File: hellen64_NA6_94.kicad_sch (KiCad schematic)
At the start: 210 parts, among them J1 USB_B_Mini, J11 Conn_01x01, J13 Conn_01x01, J14 Conn_01x01, J15 Conn_01x01, J16 Conn_01x01, J17 Conn_01x01, J19 Conn_01x01, J2 Conn_01x05_Male, J20 Conn_01x01, J21 Conn_01x01, J22 Conn_01x01, J24 Conn_01x01, J25 AudioJack3_SwitchTR, J27 Conn_01x06, J4 Conn_02x12_Odd_Even, J5 USB_B, M1 Module-input-0.1, M10 Module-power12-0.2, M11 Module-power5-0.2, M12 Module-wbo-0.3, M13 Module-can-0.1, M2 Module-ign8-0.2, M3 Module-mcu144-0.6, M4 Module-sd-0.1, M5 Module-output-0.3, M6 Module-dinput4-0.1, M7 Module-stlink-0.1, M8 Module-can-0.1, M9 Module-knock-0.1, P1 Pad, P10 Pad, P11 Pad, P12 Pad, P13 Pad, P14 Pad, P15 Pad, P16 Pad, P17 Pad, P18 Pad, P19 Pad, P2 178780-1, P20 Pad, P21 Pad, P22 Pad, P23 Pad, P24 Pad, P25 Pad, P26 Pad, P27 Pad, P28 Pad, P29 Pad, P3 Pad, P30 Pad, P31 Pad, P32 Pad, P33 Pad, P34 Pad, P35 Pad, P36 Pad, P37 Pad, P38 Pad, P39 Pad, P4 Pad, P40 Pad, P41 Pad, P42 Pad, P43 Pad, P44 Pad, P45 Pad, P5 Pad, P6 Pad, P7 Pad, P8 Pad, P9 Pad, U1 LIS2DW12TR, U2 MPX4_MAP, U3 MCP6002-xSN, U4 LPS25HB, U5 L6205PD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

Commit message: rev.C pcb (draft)
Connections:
- net +5VA: no longer P2.31 (2B), P2.44 (3K), R23.1, R31.1
- net +5VAS: now also P2.31 (2B), P2.44 (3K), R23.1, R31.1
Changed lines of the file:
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@@
   (title_block
     (title "hellen64 NA6 94")
-    (date "2022-06-17")
+    (date "2022-06-20")
     (rev "С")
     (company "rusEFI")
@@
     (pin "2")
   )
+  (symbol (lib_id "alphax:+5VAS") (at 110.49 60.96 270) (unit 1)
+    (in_bom yes) (on_board yes)
+    (property "Reference" "#PWR0148" (id 0) (at 110.49 57.15 0)
+      (effects (font (size 1.27 1.27)) hide)
+    )
+    (property "Value" "+5VAS" (id 1) (at 114.3 60.96 90)
+      (effects (font (size 1.27 1.27)) (justify left))
+    )
+    (property "Footprint" "" (id 2) (at 110.49 60.96 0)
+      (effects (font (size 1.27 1.27)) hide)
+    )
+    (property "Datasheet" "" (id 3) (at 110.49 60.96 0)
+      (effects (font (size 1.27 1.27)) hide)
+    )
+    (pin "1")
+  )
   (symbol (lib_id "178780-1:178780-1") (at 87.63 43.18 90) (unit 2)
     (in_bom yes) (on_board yes)
@@
     (pin "1")
   )
+  (symbol (lib_id "alphax:+5VAS") (at 134.62 113.03 270) (unit 1)
+    (in_bom yes) (on_board yes)
+    (property "Reference" "#PWR0103" (id 0) (at 134.62 109.22 0)
+      (effects (font (size 1.27 1.27)) hide)
+    )
+    (property "Value" "+5VAS" (id 1) (at 138.43 113.03 90)
+      (effects (font (size 1.27 1.27)) (justify left))
+    )
+    (property "Footprint" "" (id 2) (at 134.62 113.03 0)
+      (effects (font (size 1.27 1.27)) hide)
+    )
+    (property "Datasheet" "" (id 3) (at 134.62 113.03 0)
+      (effects (font (size 1.27 1.27)) hide)
+    )
+    (pin "1")
+  )
   (symbol (lib_id "Connector_Generic:Conn_01x01") (at 513.08 374.65 0) (mirror y) (unit 1)
     (in_bom yes) (on_board yes)
@@
     (pin "9")
   )
-  (symbol (lib_id "power:+5VA") (at 134.62 113.03 270) (mirror x) (unit 1)
-    (in_bom yes) (on_board yes)
-    (property "Reference" "#PWR097" (id 0) (at 130.81 113.03 0)
-      (effects (font (size 1.27 1.27)) hide)
-    )
-    (property "Value" "+5VA" (id 1) (at 135.8469 114.721 90))
-    (property "Footprint" "" (id 2) (at 134.62 113.03 0)
-      (effects (font (size 1.27 1.27)) hide)
-    )
-    (property "Datasheet" "" (id 3) (at 134.62 113.03 0)
-      (effects (font (size 1.27 1.27)) hide)
-    )
-    (pin "1")
-  )
   (symbol (lib_id "hellen-one-common:Pad") (at 290.83 300.99 180) (unit 1)
     (in_bom yes) (on_board yes)
@@
     (pin "7")
   )
-  (symbol (lib_id "power:+5VA") (at 110.49 60.96 270) (mirror x) (unit 1)
-    (in_bom yes) (on_board yes)
-    (property "Reference" "#PWR055" (id 0) (at 106.68 60.96 0)
-      (effects (font (size 1.27 1.27)) hide)
-    )
-    (property "Value" "+5VA" (id 1) (at 115.57 60.96 90))
-    (property "Footprint" "" (id 2) (at 110.49 60.96 0)
-      (effects (font (size 1.27 1.27)) hide)
-    )
-    (property "Datasheet" "" (id 3) (at 110.49 60.96 0)
-      (effects (font (size 1.27 1.27)) hide)
-    )
-    (pin "1")
-  )
   (symbol (lib_id "hellen-one-common:Jumper-Pad-Pad") (at 127 184.15 0) (mirror y) (unit 1)
     (in_bom yes) (on_board yes)
@@
     (pin "1")
   )
-  (symbol (lib_id "power:+5VA") (at 185.42 171.45 0) (mirror y) (unit 1)
-    (in_bom yes) (on_board yes)
-    (property "Reference" "#PWR0123" (id 0) (at 185.42 175.26 0)
-      (effects (font (size 1.27 1.27)) hide)
-    )
-    (property "Value" "+5VA" (id 1) (at 185.0517 167.1256 0))
-    (property "Footprint" "" (id 2) (at 185.42 171.45 0)
-      (effects (font (size 1.27 1.27)) hide)
-    )
-    (property "Datasheet" "" (id 3) (at 185.42 171.45 0)
-      (effects (font (size 1.27 1.27)) hide)
-    )
-    (pin "1")
-  )
   (symbol (lib_id "hellen-one-common:LIS2DW12TR") (at 497.84 69.85 0) (unit 1)
     (in_bom yes) (on_board yes) (fields_autoplaced)
@@
     (pin "1")
   )
+  (symbol (lib_id "alphax:+5VAS") (at 140.97 168.91 270) (unit 1)
+    (in_bom yes) (on_board yes)
+    (property "Reference" "#PWR0123" (id 0) (at 140.97 165.1 0)
+      (effects (font (size 1.27 1.27)) hide)
+    )
+    (property "Value" "+5VAS" (id 1) (at 144.78 168.91 90)
+      (effects (font (size 1.27 1.27)) (justify left))
+    )
+    (property "Footprint" "" (id 2) (at 140.97 168.91 0)
+      (effects (font (size 1.27 1.27)) hide)
+    )
+    (property "Datasheet" "" (id 3) (at 140.97 168.91 0)
+      (effects (font (size 1.27 1.27)) hide)
+    )
+    (pin "1")
+  )
   (symbol (lib_id "hellen-one-common:Pad") (at 285.75 149.86 0) (mirror y) (unit 1)
     (in_bom yes) (on_board yes)
@@
     (pin "2")
   )
-  (symbol (lib_id "power:+5VA") (at 140.97 168.91 270) (mirror x) (unit 1)
-    (in_bom yes) (on_board yes)
-    (property "Reference" "#PWR0103" (id 0) (at 137.16 168.91 0)
-      (effects (font (size 1.27 1.27)) hide)
-    )
-    (property "Value" "+5VA" (id 1) (at 145.8074 169.4092 90))
-    (property "Footprint" "" (id 2) (at 140.97 168.91 0)
-      (effects (font (size 1.27 1.27)) hide)
-    )
-    (property "Datasheet" "" (id 3) (at 140.97 168.91 0)
-      (effects (font (size 1.27 1.27)) hide)
-    )
-    (pin "1")
-  )
   (symbol (lib_id "hellen-one-dinput4-0.1:Module-dinput4-0.1") (at 314.96 290.83 0) (unit 1)
     (in_bom yes) (on_board yes)
@@
     )
   )
+  (symbol (lib_id "alphax:+5VAS") (at 185.42 171.45 0) (unit 1)
+    (in_bom yes) (on_board yes)
+    (property "Reference" "#PWR0149" (id 0) (at 181.61 171.45 0)
+      (effects (font (size 1.27 1.27)) hide)
+    )
+    (property "Value" "+5VAS" (id 1) (at 182.88 167.64 0)
+      (effects (font (size 1.27 1.27)) (justify left))
+    )
+    (property "Footprint" "" (id 2) (at 185.42 171.45 0)
+      (effects (font (size 1.27 1.27)) hide)
+    )
+    (property "Datasheet" "" (id 3) (at 185.42 171.45 0)
+      (effects (font (size 1.27 1.27)) hide)
+    )
+    (pin "1")
+  )
   (symbol (lib_id "hellen-one-common:PROTO_AREA") (at 539.75 304.8 0) (mirror y) (unit 1)
     (in_bom yes) (on_board yes)
@@
       (reference "#PWR054") (unit 1) (value "GNDA") (footprint "")
     )
-    (path "/5066f816-036b-494e-af0e-2f19a57ec17a"
-      (reference "#PWR055") (unit 1) (value "+5VA") (footprint "")
-    )
     (path "/59a75caf-a40f-4cf5-b8bb-e65ae86bec15"
       (reference "#PWR056") (unit 1) (value "+5VAS") (footprint "")
@@
       (reference "#PWR096") (unit 1) (value "GND") (footprint "")
     )
-    (path "/2f634a03-02f6-4cb4-a723-2198bc6849a8"
-      (reference "#PWR097") (unit 1) (value "+5VA") (footprint "")
-    )
     (path "/85f12dc3-c9a5-46a2-8a35-32f334558a91"
       (reference "#PWR098") (unit 1) (value "GNDA") (footprint "")
@@
       (reference "#PWR0102") (unit 1) (value "+5VA") (footprint "")
     )
-    (path "/bda29f98-c941-4e2c-9a70-937175c536d0"
-      (reference "#PWR0103") (unit 1) (value "+5VA") (footprint "")
+    (path "/26e09084-cf68-4803-b43d-1c70e8e23e15"
+      (reference "#PWR0103") (unit 1) (value "+5VAS") (footprint "")
     )
     (path "/5fe6fb57-f54b-4b13-b913-34e51ba31b59"
@@
       (reference "#PWR0122") (unit 1) (value "+3V3_IGN") (footprint "")
     )
-    (path "/896ec217-3ddf-46ba-b573-cfa104c11bdb"
-      (reference "#PWR0123") (unit 1) (value "+5VA") (footprint "")
+    (path "/9fc4bb94-47c7-4ce7-bcb5-cde71a053973"
+      (reference "#PWR0123") (unit 1) (value "+5VAS") (footprint "")
     )
     (path "/e78eb1ba-d5b2-45a8-90c6-8e293da8968e"
@@
       (reference "#PWR0147") (unit 1) (value "+5VA") (footprint "")
     )
+    (path "/1a298258-d286-46a9-94bf-20394ed116da"
+      (reference "#PWR0148") (unit 1) (value "+5VAS") (footprint "")
+    )
+    (path "/cdfe12d7-e2f6-4dcc-a7bf-2c21846dc782"
+      (reference "#PWR0149") (unit 1) (value "+5VAS") (footprint "")
+    )
     (path "/3db3a3c4-147a-4536-960f-fb25c4504d99"

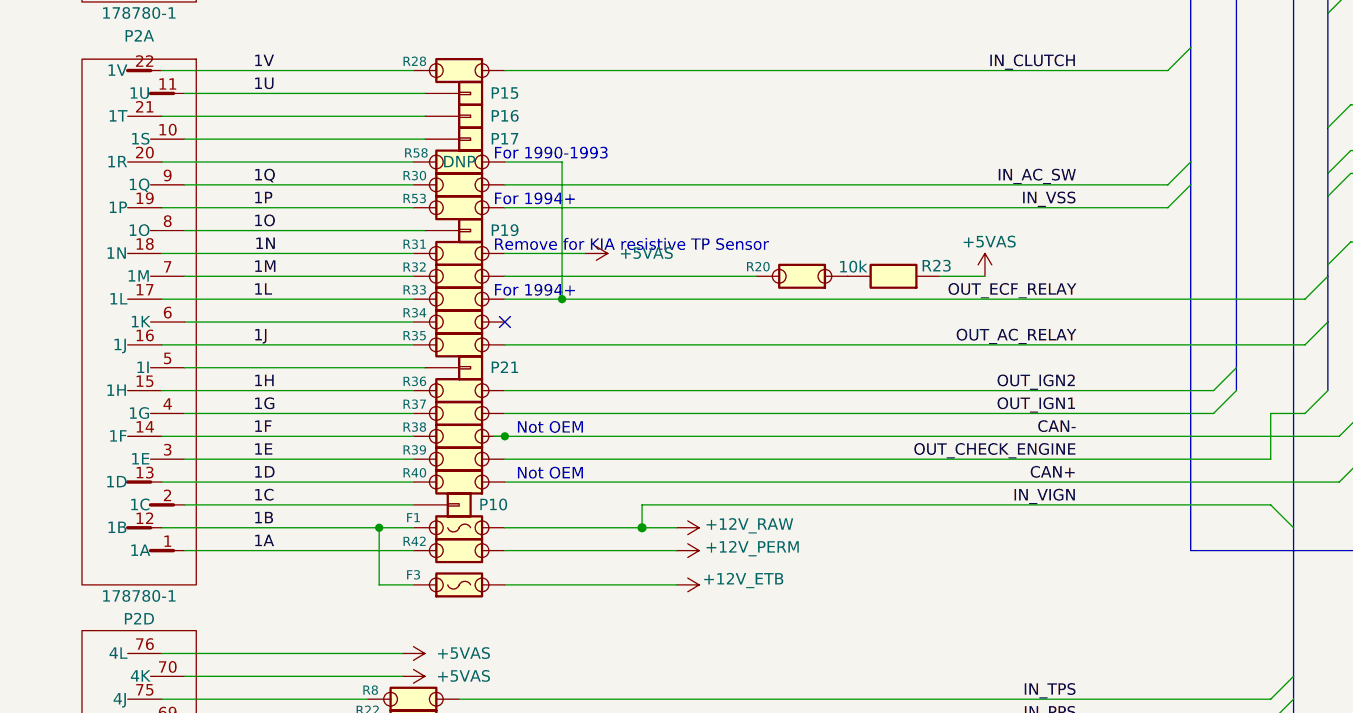
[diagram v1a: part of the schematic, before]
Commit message: VSS is on 1M https://github.com/rusefi/hellenNA6_issues/issues/26
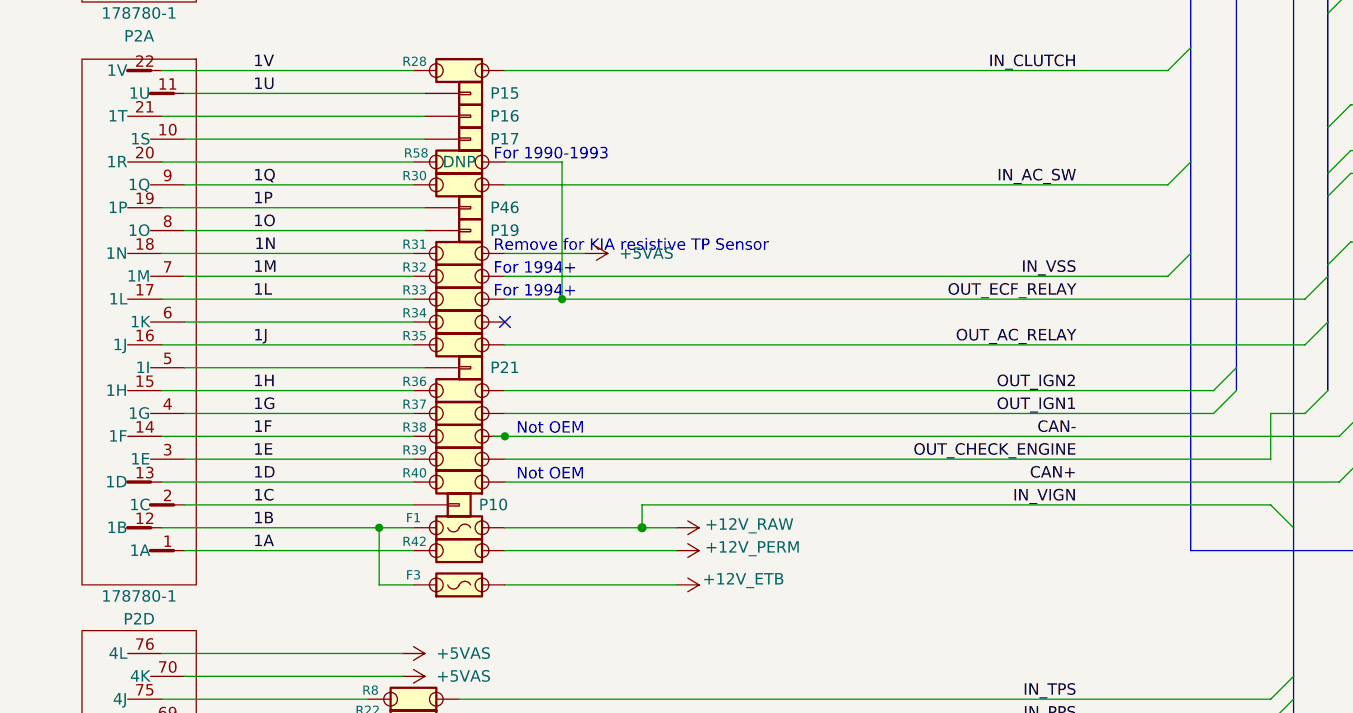
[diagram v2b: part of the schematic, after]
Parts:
- removed R20, R53: Jumper-Pad-Pad, hellen-one-common:PAD-0805-PAD, symbol hellen-one-common:Jumper-Pad-Pad
- removed R23: 10k, hellen-one-common:R0603, symbol hellen-one-common:Res
- added P46: Pad, hellen-one-common:PAD-TH, symbol hellen-one-common:Pad
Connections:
- net 1P: now also P46.1 (Pin_1)
- net IN_VSS: now also R32.1
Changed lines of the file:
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@@
   (title_block
     (title "hellen64 NA6 94")
-    (date "2022-06-20")
+    (date "2022-06-23")
     (rev "С")
     (company "rusEFI")
@@
     (stroke (width 0.1524) (type solid) (color 0 0 0 0))
   )
-  (bus_entry (at 205.74 163.83) (size 2.54 -2.54)
+  (bus_entry (at 205.74 171.45) (size 2.54 -2.54)
     (stroke (width 0.1524) (type solid) (color 0 0 0 0))
   )
@@
     (stroke (width 0.3048) (type solid) (color 0 255 255 1))
   )
-  (bus (pts (xy 208.28 201.93) (xy 208.28 161.29))
+  (bus (pts (xy 208.28 201.93) (xy 208.28 168.91))
     (stroke (width 0.3048) (type solid) (color 255 255 0 1))
   )
@@
     (stroke (width 0) (type solid) (color 0 0 0 0))
   )
-  (bus (pts (xy 208.28 161.29) (xy 208.28 158.75))
+  (bus (pts (xy 208.28 158.75) (xy 208.28 168.91))
     (stroke (width 0.3048) (type solid) (color 255 255 0 1))
   )
@@
     (stroke (width 0) (type solid) (color 0 0 0 0))
   )
-  (wire (pts (xy 132.08 163.83) (xy 205.74 163.83))
+  (wire (pts (xy 132.08 171.45) (xy 205.74 171.45))
     (stroke (width 0) (type default) (color 0 0 0 0))
   )
@@
     (stroke (width 0) (type solid) (color 0 0 0 0))
   )
-  (wire (pts (xy 185.42 171.45) (xy 180.34 171.45))
-    (stroke (width 0) (type solid) (color 0 0 0 0))
-  )
   (bus (pts (xy 381 184.15) (xy 383.54 184.15))
     (stroke (width 0) (type solid) (color 0 0 0 0))
@@
     (stroke (width 0) (type solid) (color 0 0 0 0))
   )
-  (wire (pts (xy 121.92 163.83) (xy 93.98 163.83))
+  (wire (pts (xy 123.19 163.83) (xy 93.98 163.83))
     (stroke (width 0) (type solid) (color 0 0 0 0))
   )
@@
     (stroke (width 0) (type solid) (color 0 0 0 0))
   )
-  (wire (pts (xy 160.02 171.45) (xy 132.08 171.45))
-    (stroke (width 0) (type solid) (color 0 0 0 0))
-  )
   (wire (pts (xy 93.98 223.52) (xy 116.84 223.52))
     (stroke (width 0) (type solid) (color 0 0 0 0))
@@
     (effects (font (size 1.27 1.27)) (justify left bottom))
   )
-  (text "For 1994+\n" (at 130.81 163.83 0)
+  (text "For 1994+\n" (at 130.81 171.45 0)
     (effects (font (size 1.27 1.27)) (justify left bottom))
   )
@@
     (effects (font (size 1.27 1.27)) (justify left bottom))
   )
-  (label "IN_VSS" (at 195.58 163.83 180)
+  (label "IN_VSS" (at 195.58 171.45 180)
     (effects (font (size 1.27 1.27)) (justify right bottom))
   )
@@
     (pin "1")
   )
+  (symbol (lib_id "hellen-one-common:Pad") (at 128.27 163.83 0) (mirror x) (unit 1)
+    (in_bom yes) (on_board yes)
+    (property "Reference" "P46" (id 0) (at 132.08 163.83 0))
+    (property "Value" "Pad" (id 1) (at 128.27 161.29 0)
+      (effects (font (size 1.27 1.27)) hide)
+    )
+    (property "Footprint" "hellen-one-common:PAD-TH" (id 2) (at 128.27 160.02 0)
+      (effects (font (size 1.27 1.27)) hide)
+    )
+    (property "Datasheet" "~" (id 3) (at 128.27 163.83 0)
+      (effects (font (size 1.27 1.27)) hide)
+    )
+    (pin "1")
+  )
   (symbol (lib_id "hellen-one-common:Fuse-Pad-Pad") (at 110.49 55.88 0) (unit 1)
     (in_bom yes) (on_board yes)
@@
     (pin "2")
   )
-  (symbol (lib_id "hellen-one-common:Res") (at 180.34 171.45 0) (mirror y) (unit 1)
-    (in_bom yes) (on_board yes)
-    (property "Reference" "R23" (id 0) (at 180.0421 170.3215 0))
-    (property "Value" "10k" (id 1) (at 170.7381 170.4245 0))
-    (property "Footprint" "hellen-one-common:R0603" (id 2) (at 176.53 175.26 0)
-      (effects (font (size 1.27 1.27)) hide)
-    )
-    (property "Datasheet" "" (id 3) (at 180.34 171.45 0)
-      (effects (font (size 1.27 1.27)) hide)
-    )
-    (property "LCSC" "C25804" (id 4) (at 180.34 171.45 0)
-      (effects (font (size 1.27 1.27)) hide)
-    )
-    (pin "1")
-    (pin "2")
-  )
   (symbol (lib_id "hellen-one-common:Res") (at 337.82 377.19 180) (unit 1)
     (in_bom yes) (on_board yes)
@@
     (pin "1")
   )
-  (symbol (lib_id "hellen-one-common:Jumper-Pad-Pad") (at 165.1 171.45 0) (mirror y) (unit 1)
-    (in_bom yes) (on_board yes)
-    (property "Reference" "R20" (id 0) (at 160.217 170.4186 0)
-      (effects (font (size 1.016 1.016)))
-    )
-    (property "Value" "Jumper-Pad-Pad" (id 1) (at 165.1 173.228 0)
-      (effects (font (size 1.016 1.016)) hide)
-    )
-    (property "Footprint" "hellen-one-common:PAD-0805-PAD" (id 2) (at 165.1 175.26 0)
-      (effects (font (size 1.524 1.524)) hide)
-    )
-    (property "Datasheet" "" (id 3) (at 165.1 171.45 0)
-      (effects (font (size 1.524 1.524)) hide)
-    )
-    (property "LCSC" " C17477" (id 4) (at 165.1 175.26 0)
-      (effects (font (size 1.27 1.27)) hide)
-    )
-    (pin "1")
-    (pin "2")
-  )
   (symbol (lib_id "hellen-one-mcu-0.5:Module-mcu-0.5") (at 420.37 207.01 0) (unit 3)
     (in_bom yes) (on_board yes)
@@
     )
   )
-  (symbol (lib_id "alphax:+5VAS") (at 185.42 171.45 0) (unit 1)
-    (in_bom yes) (on_board yes)
-    (property "Reference" "#PWR0149" (id 0) (at 181.61 171.45 0)
-      (effects (font (size 1.27 1.27)) hide)
-    )
-    (property "Value" "+5VAS" (id 1) (at 182.88 167.64 0)
-      (effects (font (size 1.27 1.27)) (justify left))
-    )
-    (property "Footprint" "" (id 2) (at 185.42 171.45 0)
-      (effects (font (size 1.27 1.27)) hide)
-    )
-    (property "Datasheet" "" (id 3) (at 185.42 171.45 0)
-      (effects (font (size 1.27 1.27)) hide)
-    )
-    (pin "1")
-  )
   (symbol (lib_id "hellen-one-common:PROTO_AREA") (at 539.75 304.8 0) (mirror y) (unit 1)
     (in_bom yes) (on_board yes)
@@
     (pin "2")
   )
-  (symbol (lib_id "hellen-one-common:Jumper-Pad-Pad") (at 127 163.83 0) (mirror y) (unit 1)
-    (in_bom yes) (on_board yes)
-    (property "Reference" "R53" (id 0) (at 122.0467 162.8393 0)
-      (effects (font (size 1.016 1.016)))
-    )
-    (property "Value" "Jumper-Pad-Pad" (id 1) (at 127 165.608 0)
-      (effects (font (size 1.016 1.016)) hide)
-    )
-    (property "Footprint" "hellen-one-common:PAD-0805-PAD" (id 2) (at 127 167.64 0)
-      (effects (font (size 1.524 1.524)) hide)
-    )
-    (property "Datasheet" "" (id 3) (at 127 163.83 0)
-      (effects (font (size 1.524 1.524)) hide)
-    )
-    (property "LCSC" " C17477" (id 4) (at 127 167.64 0)
-      (effects (font (size 1.27 1.27)) hide)
-    )
-    (pin "1")
-    (pin "2")
-  )
   (symbol (lib_id "power:+5V") (at 424.18 322.58 0) (unit 1)
     (in_bom yes) (on_board yes)
@@
       (reference "#PWR0148") (unit 1) (value "+5VAS") (footprint "")
     )
-    (path "/cdfe12d7-e2f6-4dcc-a7bf-2c21846dc782"
-      (reference "#PWR0149") (unit 1) (value "+5VAS") (footprint "")
-    )
     (path "/3db3a3c4-147a-4536-960f-fb25c4504d99"
       (reference "#PWR0156") (unit 1) (value "+12V_PROT") (footprint "")
@@
       (reference "P45") (unit 1) (value "Pad") (footprint "hellen-one-common:PAD-TH")
     )
+    (path "/3e9c1c63-e670-4848-9887-5e04bddf24de"
+      (reference "P46") (unit 1) (value "Pad") (footprint "hellen-one-common:PAD-TH")
+    )
     (path "/40bb54e1-9aae-440a-a5bd-751019fee77f"
       (reference "R1") (unit 1) (value "470") (footprint "hellen-one-common:R0603-4")
@@
       (reference "R19") (unit 1) (value "Jumper-Pad-Pad") (footprint "hellen-one-common:PAD-0805-PAD")
     )
-    (path "/5ef529eb-5411-43cc-aae0-febfa34377da"
-      (reference "R20") (unit 1) (value "Jumper-Pad-Pad") (footprint "hellen-one-common:PAD-0805-PAD")
-    )
     (path "/8c5ad615-e4e6-4784-8b31-224645ffb293"
       (reference "R21") (unit 1) (value "1k") (footprint "hellen-one-common:R0603")
@@
       (reference "R22") (unit 1) (value "Jumper-Pad-Pad") (footprint "hellen-one-common:PAD-0805-PAD")
     )
-    (path "/4e20d7ba-c629-4b03-a4fa-1c53eed54d3d"
-      (reference "R23") (unit 1) (value "10k") (footprint "hellen-one-common:R0603")
-    )
     (path "/135d42e7-68df-4b57-b85d-22500875612c"
       (reference "R24") (unit 1) (value "Jumper-Pad-Pad") (footprint "hellen-one-common:PAD-0805-PAD")
@@
       (reference "R52") (unit 1) (value "Jumper-Pad-Pad") (footprint "hellen-one-common:PAD-0805-PAD")
     )
-    (path "/e2b89d8b-d437-40bd-adb8-b35fd77c02ad"
-      (reference "R53") (unit 1) (value "Jumper-Pad-Pad") (footprint "hellen-one-common:PAD-0805-PAD")
-    )
     (path "/587cbcb9-e1f4-47f2-a880-f0f2fe9e4f8c"
